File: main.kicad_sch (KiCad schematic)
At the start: 28 parts, among them J1 USB_C_Receptacle_USB2.0_16P, J2 Conn_ARM_JTAG_SWD_10, U1 XC6206PxxxMR, U2 USBLC6-2SC6, U3 CH340N, U4 E73-2G4M04S1B

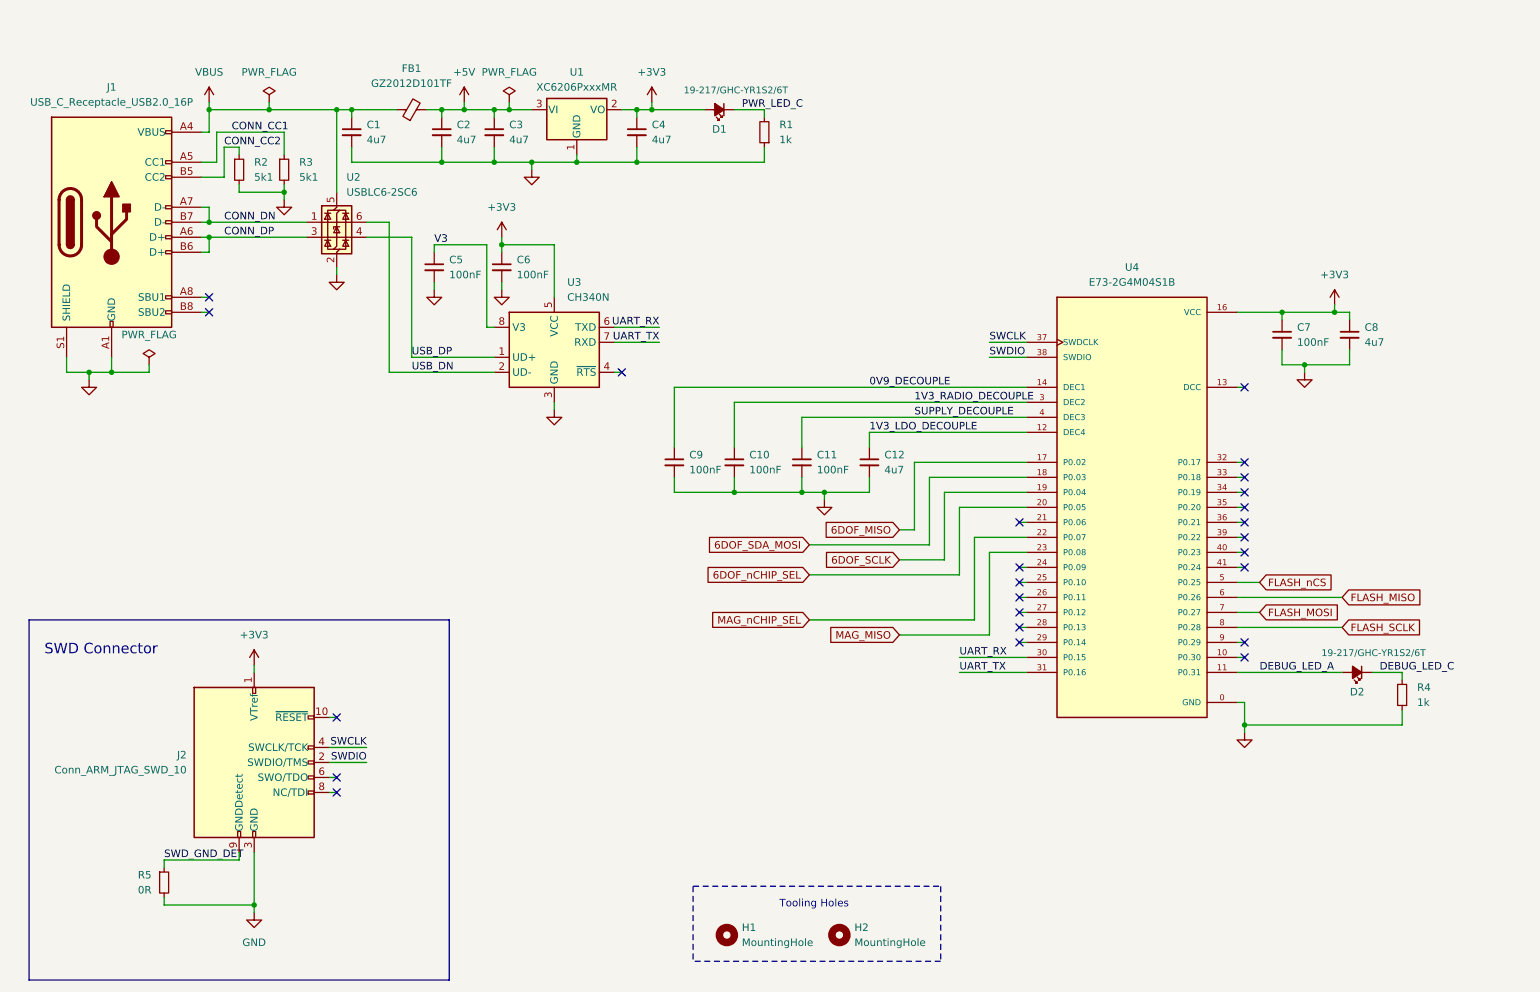
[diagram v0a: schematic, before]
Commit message: Routed diff pairs, IMU sensors, SPI Flash
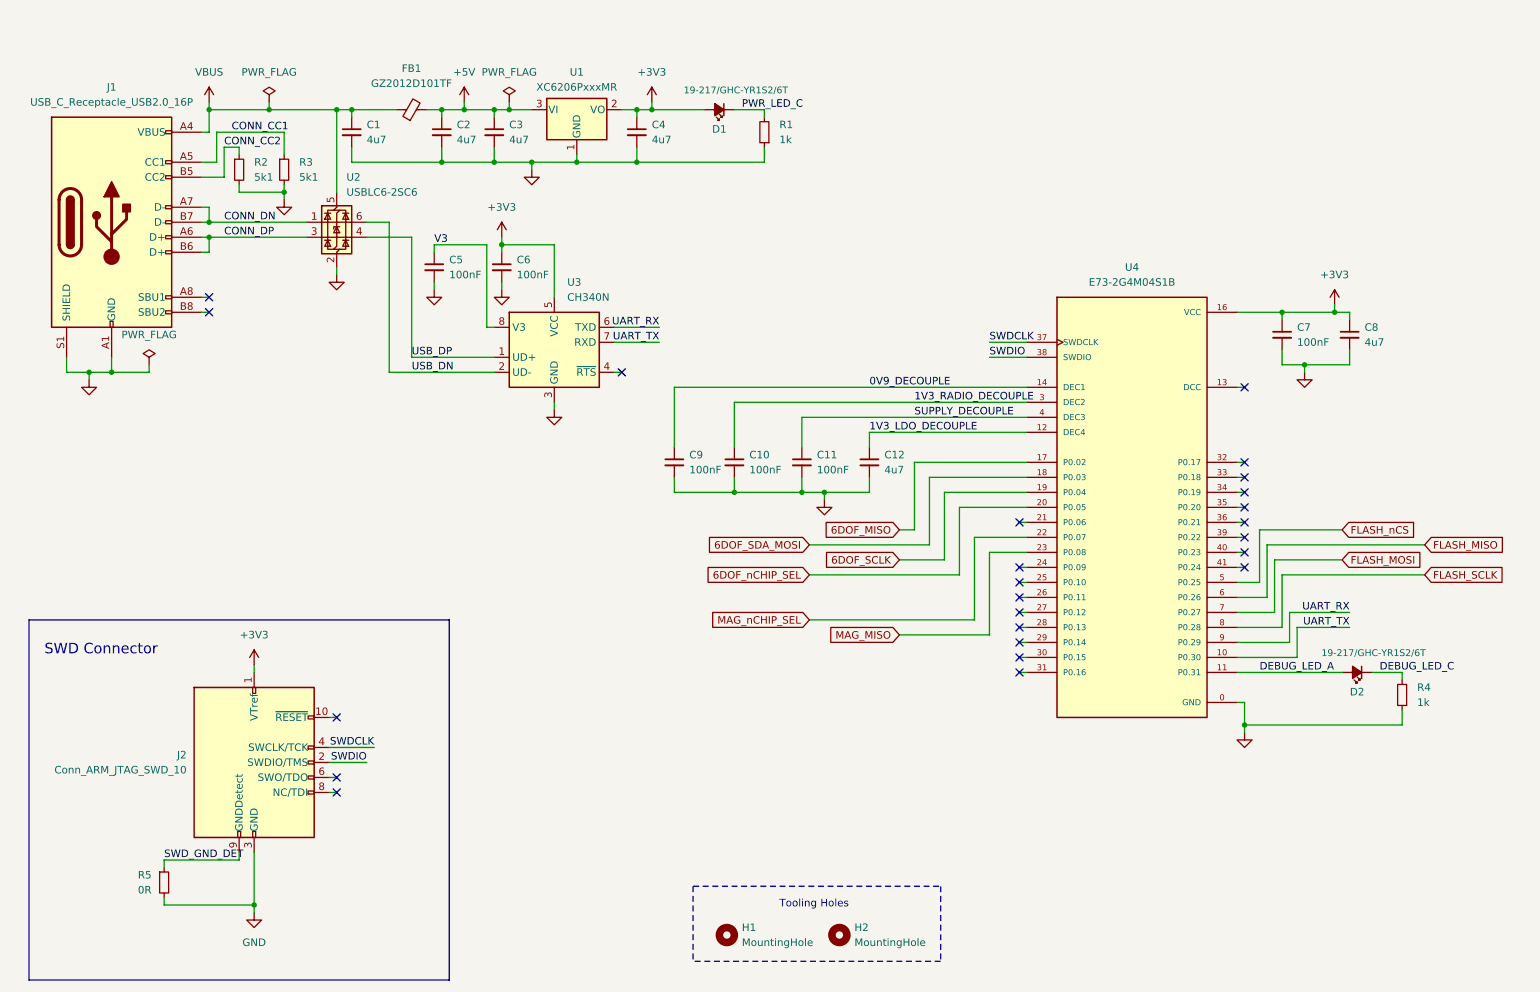
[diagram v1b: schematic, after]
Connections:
- net UART_RX: now also U4.9 (P0.29); no longer U4.30 (P0.15)
- net UART_TX: now also U4.10 (P0.30); no longer U4.31 (P0.16)
- net SWCLK renamed SWDCLK

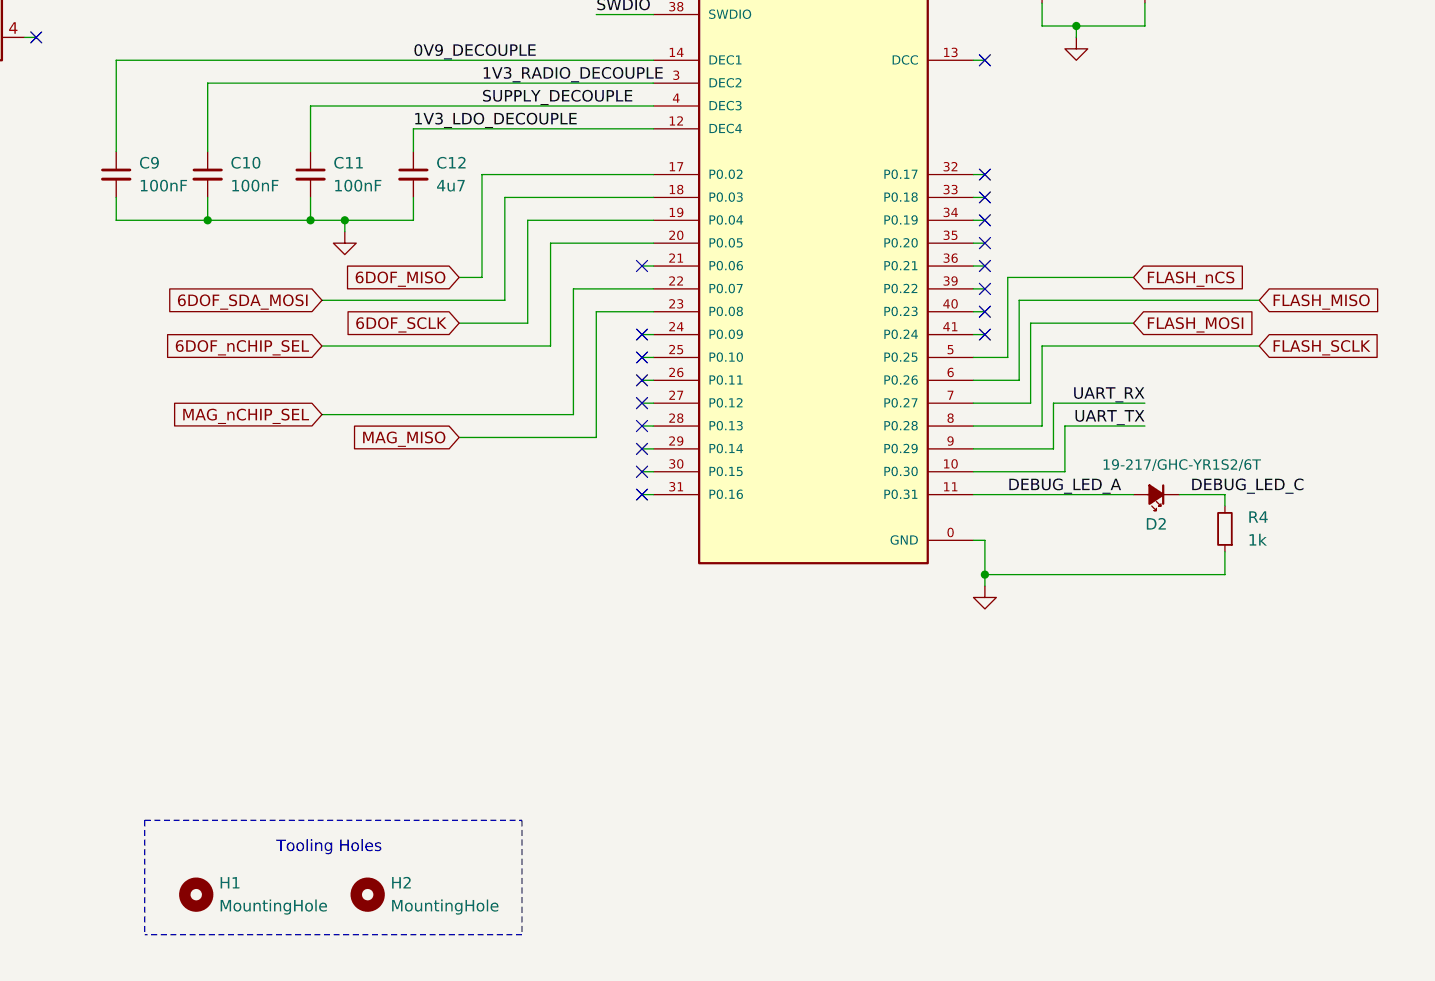
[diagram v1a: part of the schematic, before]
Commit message: Added an I2C IO expander, plus 2 pushbuttons and  2 LEDs controlled by the expander
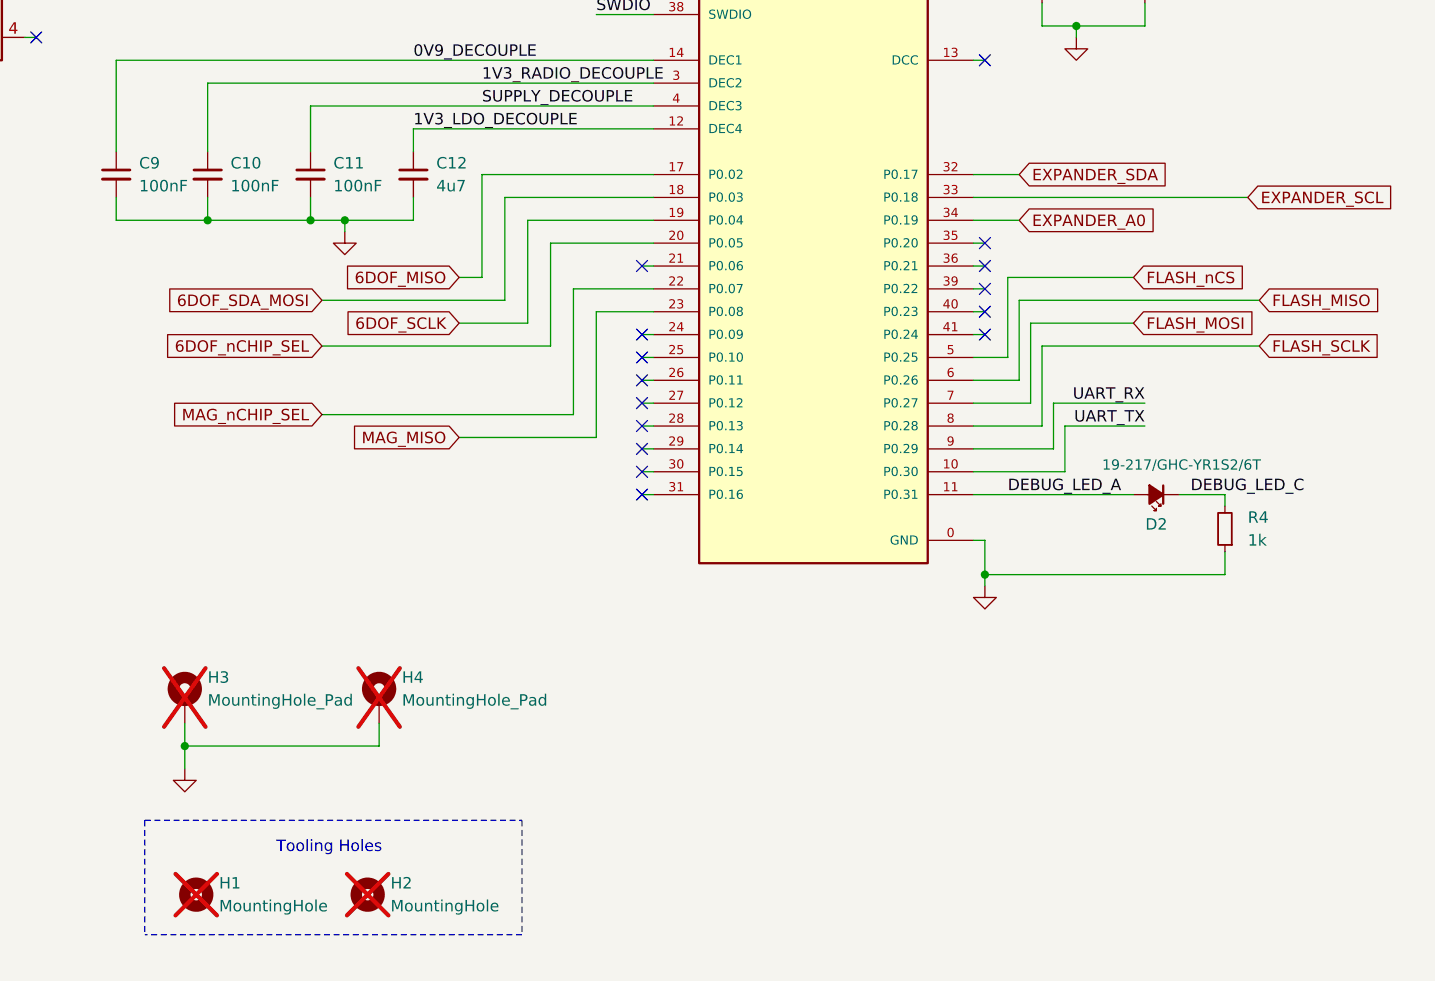
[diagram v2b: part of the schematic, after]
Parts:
- added H3, H4: MountingHole_Pad, MountingHole:MountingHole_2.2mm_M2_Pad, symbol Mechanical:MountingHole_Pad
- H1, H2: now not fitted
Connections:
- net GND: now also H3.1, H4.1
- net EXPANDER_SDA: now reaches U4.32 (P0.17)
- net EXPANDER_SCL: now reaches U4.33 (P0.18)
- net EXPANDER_A0: now reaches U4.34 (P0.19)
- no-connect marks 24 -> 21
